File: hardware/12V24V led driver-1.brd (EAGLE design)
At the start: 38.4 x 9.2 mm, 30 parts, among them X1 USB-MICROB

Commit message: usb ctrl imp.
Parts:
- removed CTRL, GND, UC1, UC2, UC3: (no value), SparkFun:1X01NS
- removed JP1: MISO, bicyclelab:PAD-SMD
- removed JP3: SCK, bicyclelab:PAD-SMD
- removed JP4: RESET, bicyclelab:PAD-SMD
- removed JP5: MOSI, bicyclelab:PAD-SMD
- removed JP6: GND, bicyclelab:PAD-SMD
- removed JP9: VCC, bicyclelab:PAD-SMD
- C1: value 1uF -> 4u7F
- MISB-SW-5B: value USB-MICROB -> MISB-SW-5B
- R1: value 100k -> 10k
- UC4: device SparkFun:1X01NS -> SparkFun:PAD-1.5X4.5
- moved JP7 21.2 mm to (21.9, 7.30), turned to 270 degrees
- moved JP2 2.22 mm to (36.5, 1.91)
- moved LGND 2.22 mm to (36.5, 5.40)
- moved C1 2.22 mm to (24.8, 3.49)
- moved C2 2.22 mm to (33.3, 3.17)
- moved C3 2.22 mm to (27.3, 7.30)
- moved L1 2.22 mm to (27.6, 1.91)
- moved R2 2.22 mm to (32.7, 7.62)
- moved R3 2.22 mm to (25.7, 7.30)
- moved U$1 2.22 mm to (30.2, 3.81)
- moved UC4 0.32 mm to (16.8, 2.22), turned to 90 degrees
- renumbered X1 to MISB-SW-5B
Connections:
- removed net GND1: JP6.P$1
- net !RST: now also JP7.4; no longer JP4.P$1
- net 5VCC: now also JP7.6; no longer JP9.P$1
- net A3/D3: now also UC4.P$1; no longer UC4.1
- net CTRL: no longer CTRL.1
- net GND: now also JP7.5; no longer GND.1
- net MISO/PWM1: now also JP7.2; no longer JP1.P$1, UC2.1
- net MOSI: now also JP7.1; no longer JP5.P$1, UC1.1
- net SCK/INT0: now also JP7.3; no longer JP3.P$1, UC3.1
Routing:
- net !RST: track 0.00 -> 12.6 mm
- net MOSI: track 12.7 -> 18.4 mm, vias 1 -> 2
- net 5VCC: track 48.5 -> 54.2 mm, vias 5 -> 6
- net SCK/INT0: track 13.6 -> 18.7 mm
- net MISO/PWM1: track 12.6 -> 13.3 mm

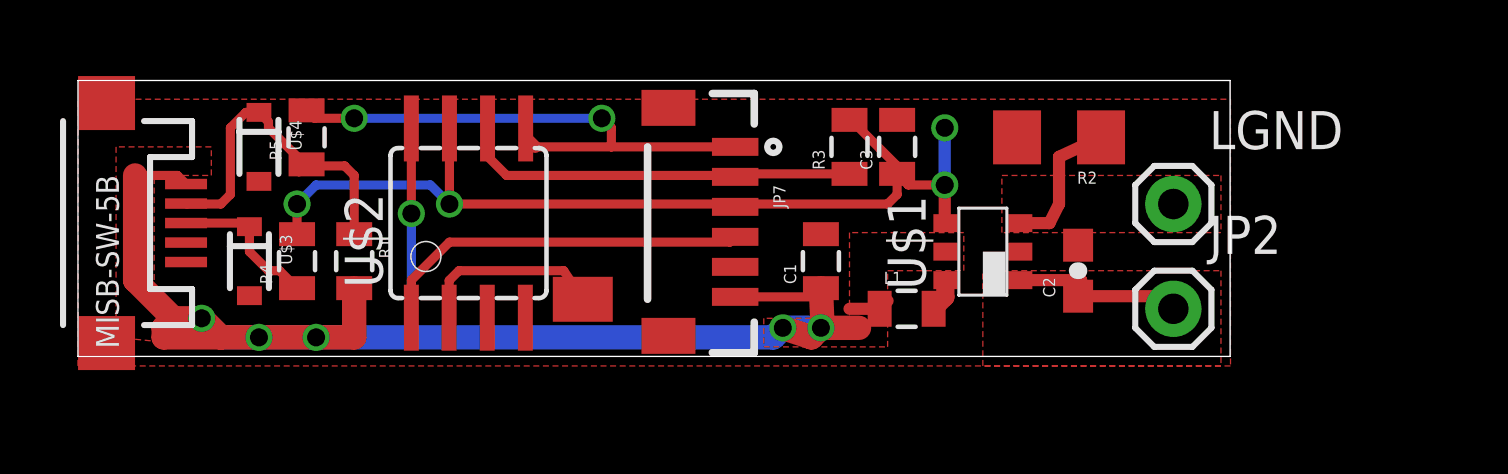
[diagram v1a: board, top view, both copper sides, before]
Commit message: usb ctrl imp.
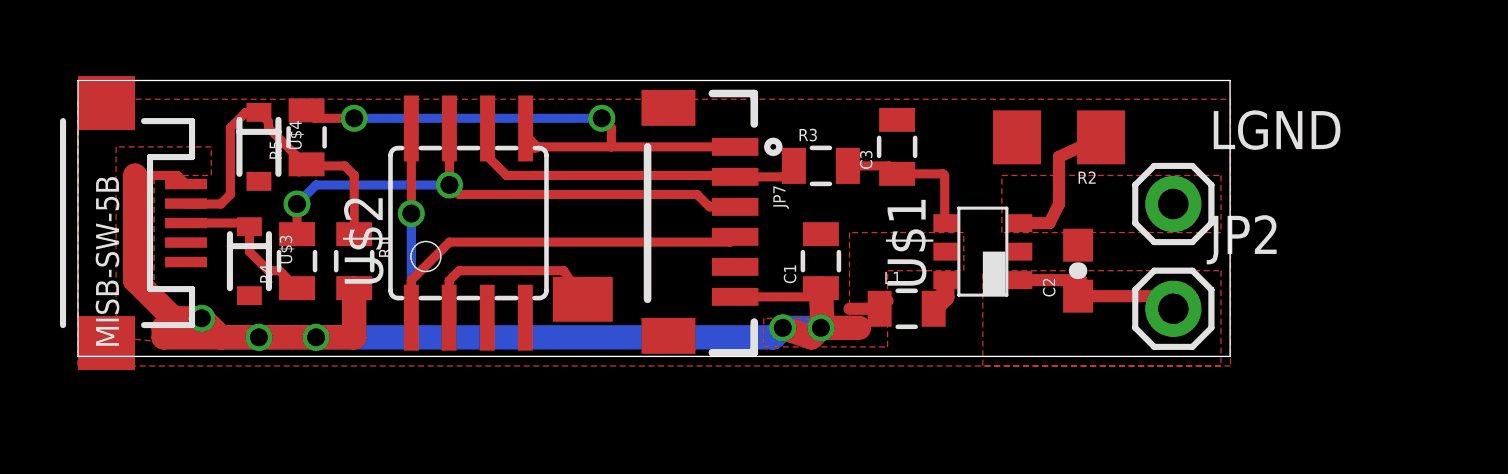
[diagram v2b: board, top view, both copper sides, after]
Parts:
- moved R3 1.14 mm to (24.8, 6.67), turned to 0 degrees
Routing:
- net CTRL: track 13.6 -> 4.96 mm, vias 2 -> 0
- net MISO/PWM1: track 13.3 -> 11.7 mm
- net SCK/INT0: track 18.7 -> 18.2 mm
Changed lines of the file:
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@@
 <element name="MISB-SW-5B" library="0-SparkFun" package="USB-MICROB" value="MISB-SW-5B" x="0.9525" y="4.7625" rot="R270"/>
 <element name="U$2" library="0-avr-7" package="SOIC8" value="tiny45" x="13.0175" y="4.7625"/>
-<element name="R3" library="SparkFun" package="0805" value="5k" x="25.7175" y="7.3025" rot="R90"/>
+<element name="R3" library="SparkFun" package="0805" value="5k" x="24.765" y="6.6675"/>
 <element name="C3" library="SparkFun" package="0805" value="0.22uF" x="27.305" y="7.3025" rot="R90"/>
 <element name="UC4" library="SparkFun" package="PAD-1.5X4.5" value="" x="16.8275" y="2.2225" rot="R90"/>
@@
 </polygon>
 <contactref element="JP7" pad="5"/>
-<wire x1="24.765" y1="4.3925" x2="27.305" y2="8.2025" width="0" layer="19" extent="1-1"/>
 <wire x1="5.715" y1="2.3425" x2="14.9125" y2="1.6085" width="0" layer="19" extent="1-1"/>
 </signal>
@@
 <contactref element="R3" pad="2"/>
 <contactref element="C3" pad="1"/>
-<wire x1="28.8925" y1="6.0325" x2="28.8925" y2="4.78" width="0.4064" layer="1"/>
-<wire x1="28.8925" y1="4.78" x2="28.9125" y2="4.76" width="0.4064" layer="1"/>
-<wire x1="28.8925" y1="7.9375" x2="28.8925" y2="6.0325" width="0.4064" layer="16"/>
-<via x="28.8925" y="6.0325" extent="1-16" drill="0.6" shape="square"/>
-<via x="28.8925" y="7.9375" extent="1-16" drill="0.6" shape="square"/>
-<wire x1="27.305" y1="6.4025" x2="27.305" y2="5.715" width="0.3048" layer="1"/>
-<wire x1="27.305" y1="5.715" x2="26.9875" y2="5.3975" width="0.3048" layer="1"/>
-<wire x1="25.7175" y1="8.2025" x2="25.77" y2="8.2025" width="0.3048" layer="1"/>
-<wire x1="25.77" y1="8.2025" x2="27.305" y2="6.6675" width="0.3048" layer="1"/>
-<wire x1="27.305" y1="6.6675" x2="27.305" y2="6.4025" width="0.3048" layer="1"/>
-<wire x1="27.305" y1="6.4025" x2="27.675" y2="6.0325" width="0.3048" layer="1"/>
-<wire x1="27.675" y1="6.0325" x2="28.8925" y2="6.0325" width="0.3048" layer="1"/>
-<wire x1="26.9875" y1="5.3975" x2="22.5425" y2="5.3975" width="0.3048" layer="1"/>
-<wire x1="21.9075" y1="5.3975" x2="22.5425" y2="5.3975" width="0.3048" layer="1"/>
+<wire x1="28.9125" y1="4.76" x2="28.8925" y2="4.78" width="0.3048" layer="1"/>
+<wire x1="28.8925" y1="4.78" x2="28.8925" y2="6.35" width="0.3048" layer="1"/>
+<wire x1="28.8925" y1="6.35" x2="28.84" y2="6.4025" width="0.3048" layer="1"/>
+<wire x1="28.84" y1="6.4025" x2="27.305" y2="6.4025" width="0.3048" layer="1"/>
+<wire x1="27.305" y1="6.4025" x2="27.04" y2="6.6675" width="0.3048" layer="1"/>
+<wire x1="27.04" y1="6.6675" x2="25.665" y2="6.6675" width="0.3048" layer="1"/>
 </signal>
 <signal name="5VCC">
@@
 <wire x1="13.6525" y1="6.985" x2="13.6525" y2="7.9165" width="0.3048" layer="1"/>
 <wire x1="21.9075" y1="6.3025" x2="22.0075" y2="6.4025" width="0.3048" layer="1"/>
-<wire x1="22.0075" y1="6.4025" x2="25.7175" y2="6.4025" width="0.3048" layer="1"/>
+<wire x1="23.865" y1="6.6675" x2="23.5" y2="6.3025" width="0.3048" layer="1"/>
+<wire x1="23.5" y1="6.3025" x2="21.9075" y2="6.3025" width="0.3048" layer="1"/>
 </signal>
 <signal name="SCK/INT0">
@@
 <wire x1="7.3025" y1="4.3925" x2="7.3025" y2="5.3975" width="0.3048" layer="1"/>
 <via x="7.3025" y="5.3975" extent="1-16" drill="0.6"/>
-<via x="12.3825" y="5.3975" extent="1-16" drill="0.6"/>
-<wire x1="12.3825" y1="5.3975" x2="12.3825" y2="7.9165" width="0.3048" layer="1"/>
+<via x="12.3825" y="6.0325" extent="1-16" drill="0.6"/>
+<wire x1="12.3825" y1="6.0325" x2="12.3825" y2="7.9165" width="0.3048" layer="1"/>
 <contactref element="JP7" pad="3"/>
 <wire x1="21.9075" y1="5.3025" x2="21.8125" y2="5.3975" width="0.3048" layer="1"/>
-<wire x1="21.8125" y1="5.3975" x2="12.3825" y2="5.3975" width="0.3048" layer="1"/>
-<wire x1="12.3825" y1="5.3975" x2="11.7475" y2="6.0325" width="0.3048" layer="16"/>
-<wire x1="11.7475" y1="6.0325" x2="7.9375" y2="6.0325" width="0.3048" layer="16"/>
+<wire x1="12.3825" y1="6.0325" x2="7.9375" y2="6.0325" width="0.3048" layer="16"/>
 <wire x1="7.9375" y1="6.0325" x2="7.3025" y2="5.3975" width="0.3048" layer="16"/>
+<wire x1="12.3825" y1="6.0325" x2="12.7" y2="5.715" width="0.3048" layer="1"/>
+<wire x1="12.7" y1="5.715" x2="20.6375" y2="5.715" width="0.3048" layer="1"/>
+<wire x1="20.6375" y1="5.715" x2="21.05" y2="5.3025" width="0.3048" layer="1"/>
+<wire x1="21.05" y1="5.3025" x2="21.9075" y2="5.3025" width="0.3048" layer="1"/>
 </signal>
 <signal name="A3/D3">
